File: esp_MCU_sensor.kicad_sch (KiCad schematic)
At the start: 38 parts, among them J4 Conn_01x04_Pin, SW1 SW_Push, U1 ESP32-S3, U2 MX25L6433FM2I-08G, U3 ESP-PSRAM32, U4 BMI323, Y1 Crystal_GND24

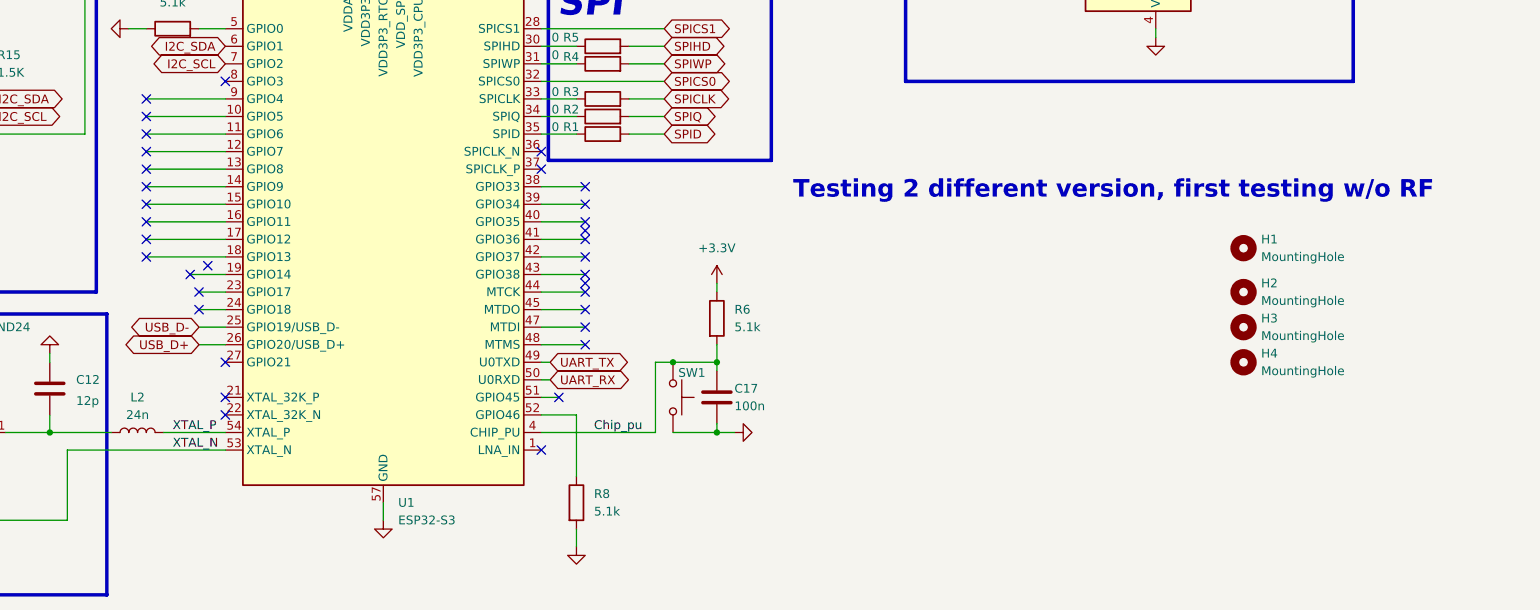
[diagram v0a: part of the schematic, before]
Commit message: Add RF schematics for GPS + designed Pi filter for imp matching
added impedance matching on LNA 1 pin, added GPS/GNSS IC
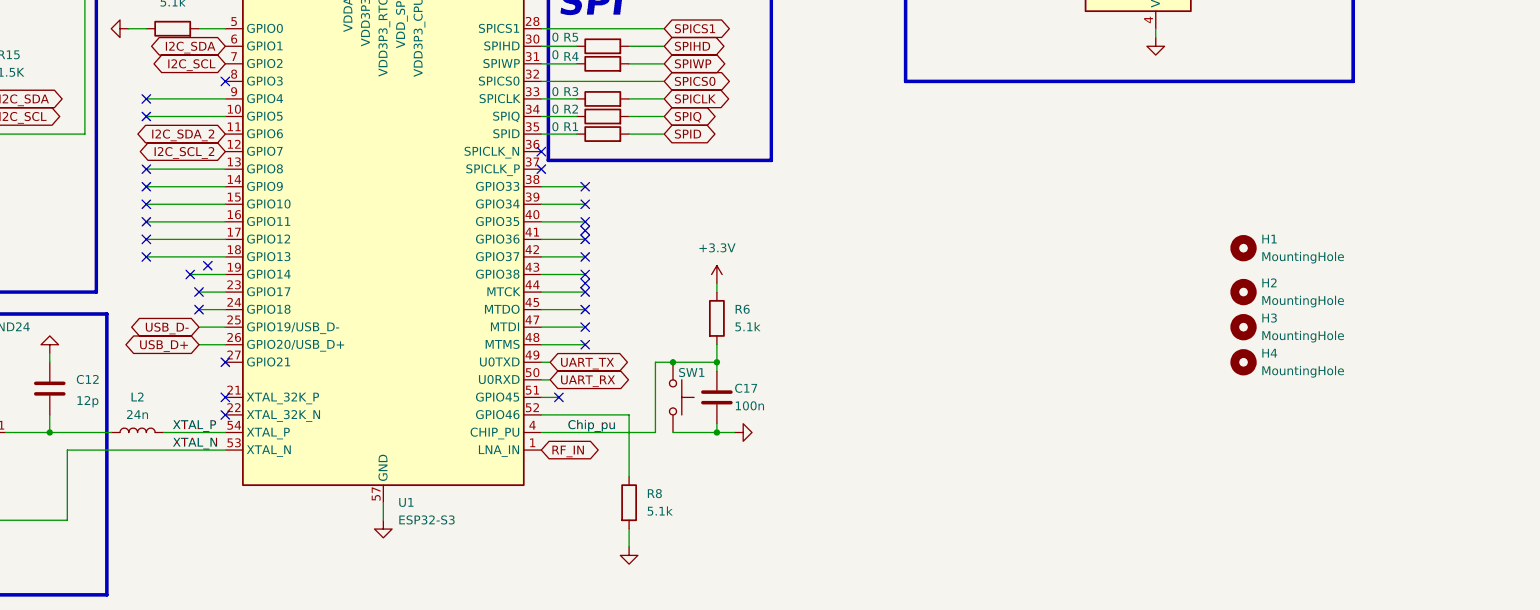
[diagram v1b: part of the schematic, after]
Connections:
- net RF_IN: now reaches U1.1 (LNA_IN)
- net I2C_SDA_2: now reaches U1.11 (GPIO6)
- net I2C_SCL_2: now reaches U1.12 (GPIO7)
- no-connect marks 36 -> 33
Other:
- note removed: "Testing 2 different version, first testing w/o RF"
- moved on the sheet: R8
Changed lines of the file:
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@@
 		)
 	)
-	(text "Testing 2 different version, first testing w/o RF\n"
-		(exclude_from_sim no)
-		(at 232.664 110.998 0)
-		(effects
-			(font
-				(size 2.54 2.54)
-				(thickness 0.508)
-				(bold yes)
-			)
-		)
-	)
 	(text "500mA\n"
 		(exclude_from_sim no)
@@
 	)
 	(no_connect
-		(at 92.71 105.41)
-	)
-	(no_connect
 		(at 64.77 110.49)
 	)
@@
 	)
 	(no_connect
-		(at 149.86 148.59)
-	)
-	(no_connect
 		(at 100.33 128.27)
 	)
 	(no_connect
-		(at 92.71 102.87)
-	)
-	(no_connect
 		(at 104.14 135.89)
 	)
@@
 	(wire
 		(pts
-			(xy 154.94 143.51) (xy 154.94 152.4)
+			(xy 162.56 143.51) (xy 162.56 152.4)
 		)
 		(stroke
@@
 	(wire
 		(pts
-			(xy 149.86 143.51) (xy 154.94 143.51)
+			(xy 149.86 143.51) (xy 162.56 143.51)
 		)
 		(stroke
@@
 	(wire
 		(pts
-			(xy 154.94 160.02) (xy 154.94 162.56)
+			(xy 162.56 160.02) (xy 162.56 162.56)
 		)
 		(stroke
@@
 	(wire
 		(pts
-			(xy 92.71 105.41) (xy 104.14 105.41)
-		)
-		(stroke
-			(width 0)
-			(type default)
-		)
-	)
-	(wire
-		(pts
 			(xy 78.74 143.51) (xy 78.74 146.05)
 		)
@@
 	(wire
 		(pts
-			(xy 92.71 102.87) (xy 104.14 102.87)
-		)
-		(stroke
-			(width 0)
-			(type default)
-		)
-	)
-	(wire
-		(pts
 			(xy 104.14 148.59) (xy 81.28 148.59)
 		)
@@
 	)
 	(label "Chip_pu"
-		(at 157.48 146.05 0)
+		(at 153.67 146.05 0)
 		(effects
 			(font
@@
 		)
 	)
+	(global_label "RF_IN"
+		(shape bidirectional)
+		(at 149.86 148.59 0)
+		(fields_autoplaced yes)
+		(effects
+			(font
+				(size 1.27 1.27)
+			)
+			(justify left)
+		)
+		(property "Intersheetrefs" "${INTERSHEET_REFS}"
+			(at 159.218 148.59 0)
+			(effects
+				(font
+					(size 1.27 1.27)
+				)
+				(justify left)
+				(hide yes)
+			)
+		)
+	)
 	(global_label "SPICLK"
 		(shape bidirectional)
@@
 		)
 	)
+	(global_label "I2C_SDA_2"
+		(shape bidirectional)
+		(at 104.14 102.87 180)
+		(fields_autoplaced yes)
+		(effects
+			(font
+				(size 1.27 1.27)
+			)
+			(justify right)
+		)
+		(property "Intersheetrefs" "${INTERSHEET_REFS}"
+			(at 90.2464 102.87 0)
+			(effects
+				(font
+					(size 1.27 1.27)
+				)
+				(justify right)
+				(hide yes)
+			)
+		)
+	)
+	(global_label "I2C_SCL_2"
+		(shape bidirectional)
+		(at 104.14 105.41 180)
+		(fields_autoplaced yes)
+		(effects
+			(font
+				(size 1.27 1.27)
+			)
+			(justify right)
+		)
+		(property "Intersheetrefs" "${INTERSHEET_REFS}"
+			(at 90.3069 105.41 0)
+			(effects
+				(font
+					(size 1.27 1.27)
+				)
+				(justify right)
+				(hide yes)
+			)
+		)
+	)
 	(global_label "I2C_SCL"
 		(shape bidirectional)
@@
 	(symbol
 		(lib_id "power:GND")
-		(at 154.94 162.56 0)
+		(at 162.56 162.56 0)
 		(unit 1)
 		(exclude_from_sim no)
@@
 		(fields_autoplaced yes)
 		(property "Reference" "#PWR032"
-			(at 154.94 168.91 0)
+			(at 162.56 168.91 0)
 			(effects
 				(font
@@
 		)
 		(property "Value" "GND"
-			(at 154.94 167.64 0)
+			(at 162.56 167.64 0)
 			(effects
 				(font
@@
 		)
 		(property "Footprint" ""
-			(at 154.94 162.56 0)
+			(at 162.56 162.56 0)
 			(effects
 				(font
@@
 		)
 		(property "Datasheet" ""
-			(at 154.94 162.56 0)
+			(at 162.56 162.56 0)
 			(effects
 				(font
@@
 		)
 		(property "Description" "Power symbol creates a global label with name \"GND\" , ground"
-			(at 154.94 162.56 0)
+			(at 162.56 162.56 0)
 			(effects
 				(font
@@
 	(symbol
 		(lib_id "Device:R")
-		(at 154.94 156.21 0)
+		(at 162.56 156.21 0)
 		(unit 1)
 		(exclude_from_sim no)
@@
 		(fields_autoplaced yes)
 		(property "Reference" "R8"
-			(at 157.48 154.9399 0)
+			(at 165.1 154.9399 0)
 			(effects
 				(font
@@
 		)
 		(property "Value" "5.1k"
-			(at 157.48 157.4799 0)
+			(at 165.1 157.4799 0)
 			(effects
 				(font
@@
 		)
 		(property "Footprint" "Resistor_SMD:R_0402_1005Metric_Pad0.72x0.64mm_HandSolder"
-			(at 153.162 156.21 90)
+			(at 160.782 156.21 90)
 			(effects
 				(font
@@
 		)
 		(property "Datasheet" "~"
-			(at 154.94 156.21 0)
+			(at 162.56 156.21 0)
 			(effects
 				(font
@@
 		)
 		(property "Description" "Resistor"
-			(at 154.94 156.21 0)
+			(at 162.56 156.21 0)
 			(effects
 				(font

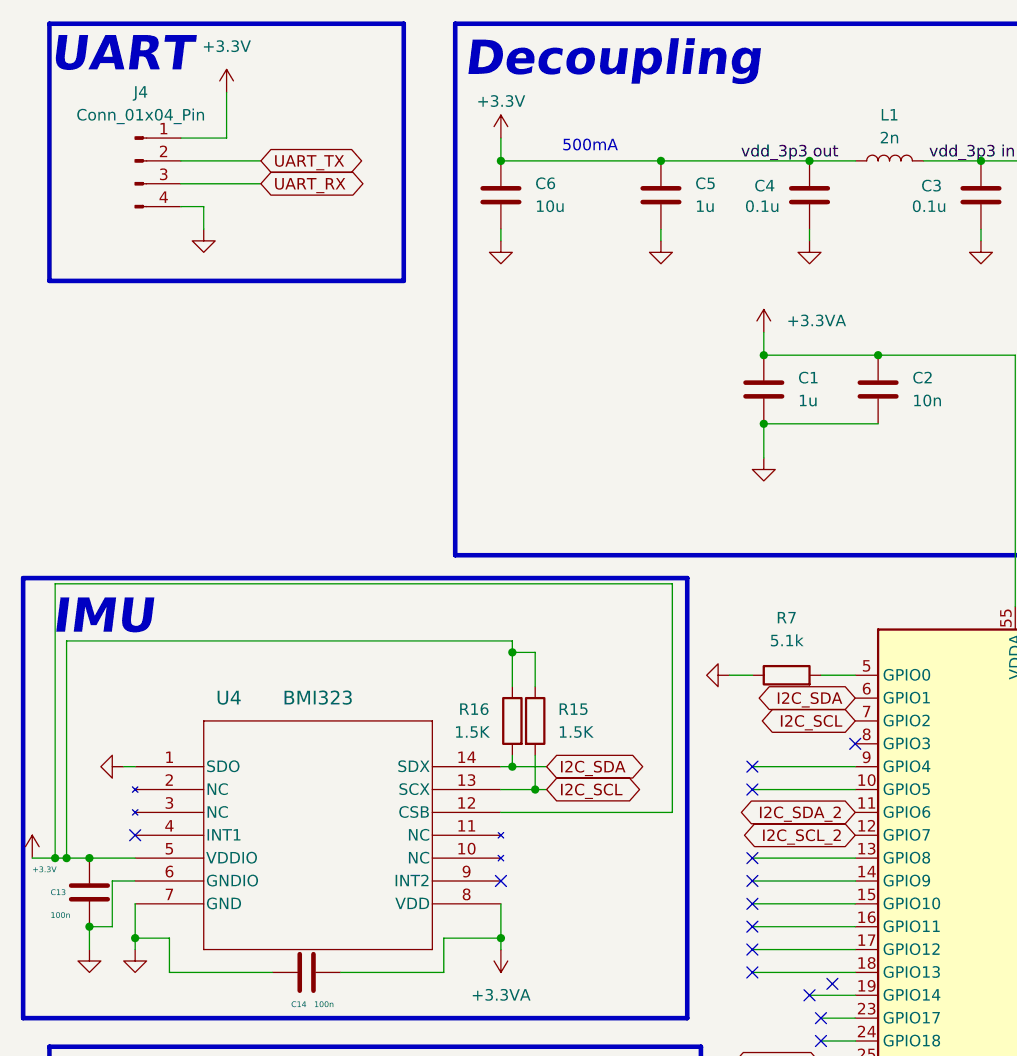
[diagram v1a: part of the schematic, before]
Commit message: Added antenna design
added pcb antenna design
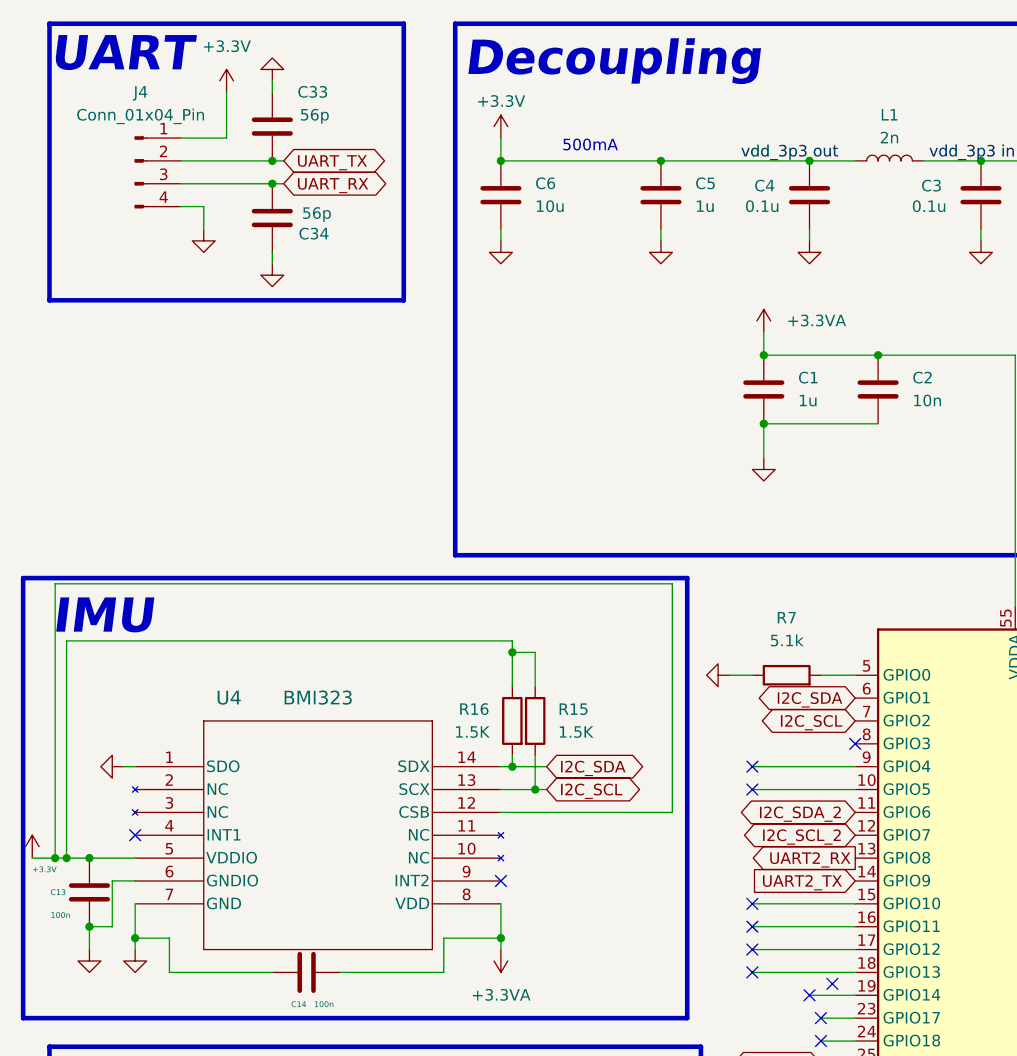
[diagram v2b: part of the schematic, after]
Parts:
- added C33, C34: 56p, Capacitor_SMD:C_0402_1005Metric_Pad0.74x0.62mm_HandSolder, symbol Device:C
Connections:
- net GND: now also C33.1, C34.1
- net UART_RX: now also C34.2
- net UART_TX: now also C33.2
- net UART2_RX: now reaches U1.13 (GPIO8)
- net UART2_TX: now reaches U1.14 (GPIO9)
- no-connect marks 33 -> 31

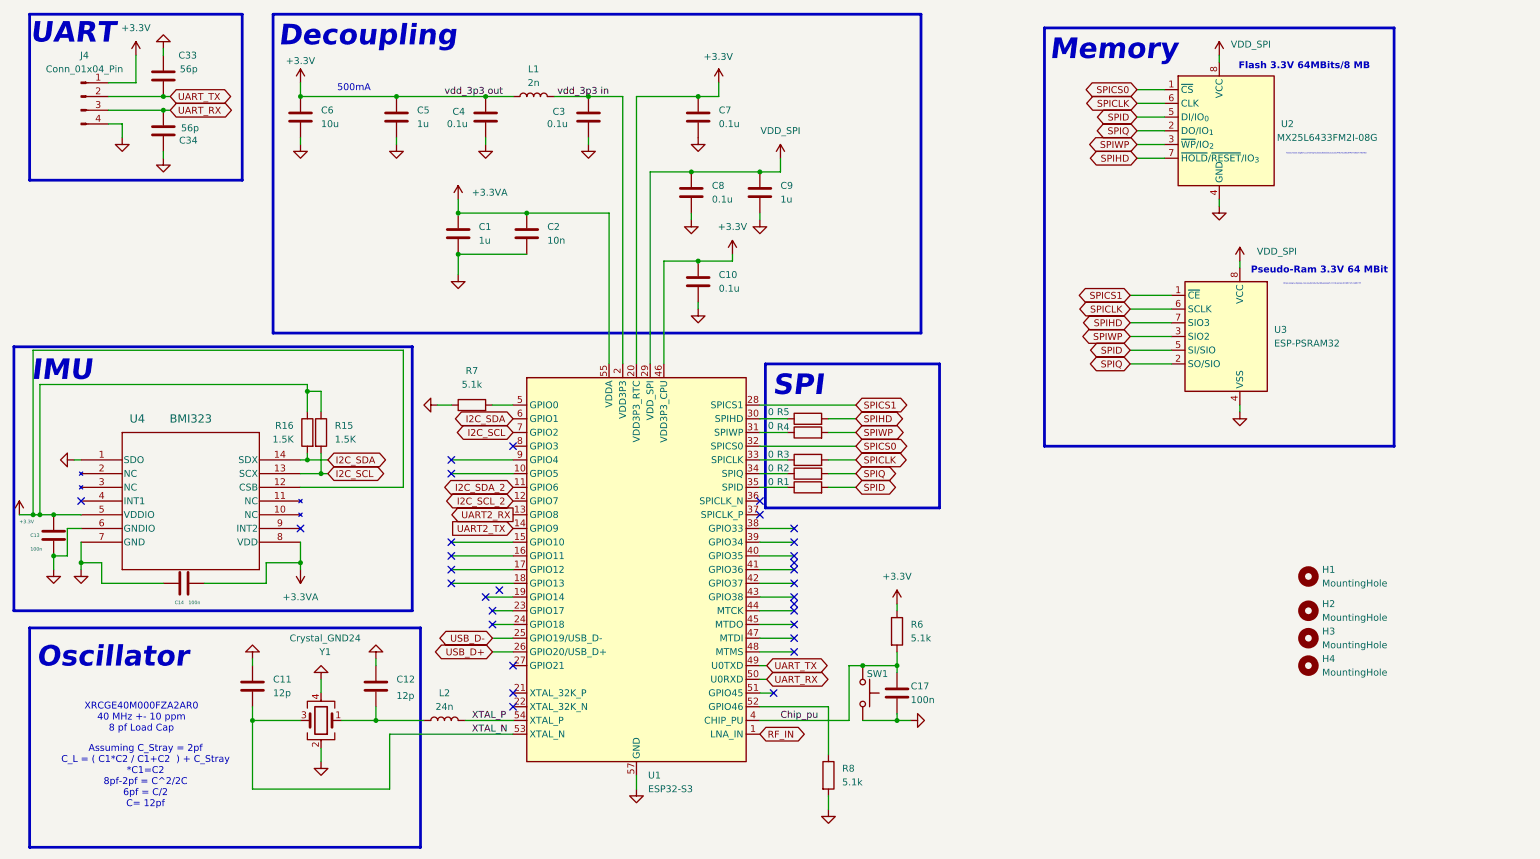
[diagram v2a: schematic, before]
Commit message: placement done
placement done, routing left
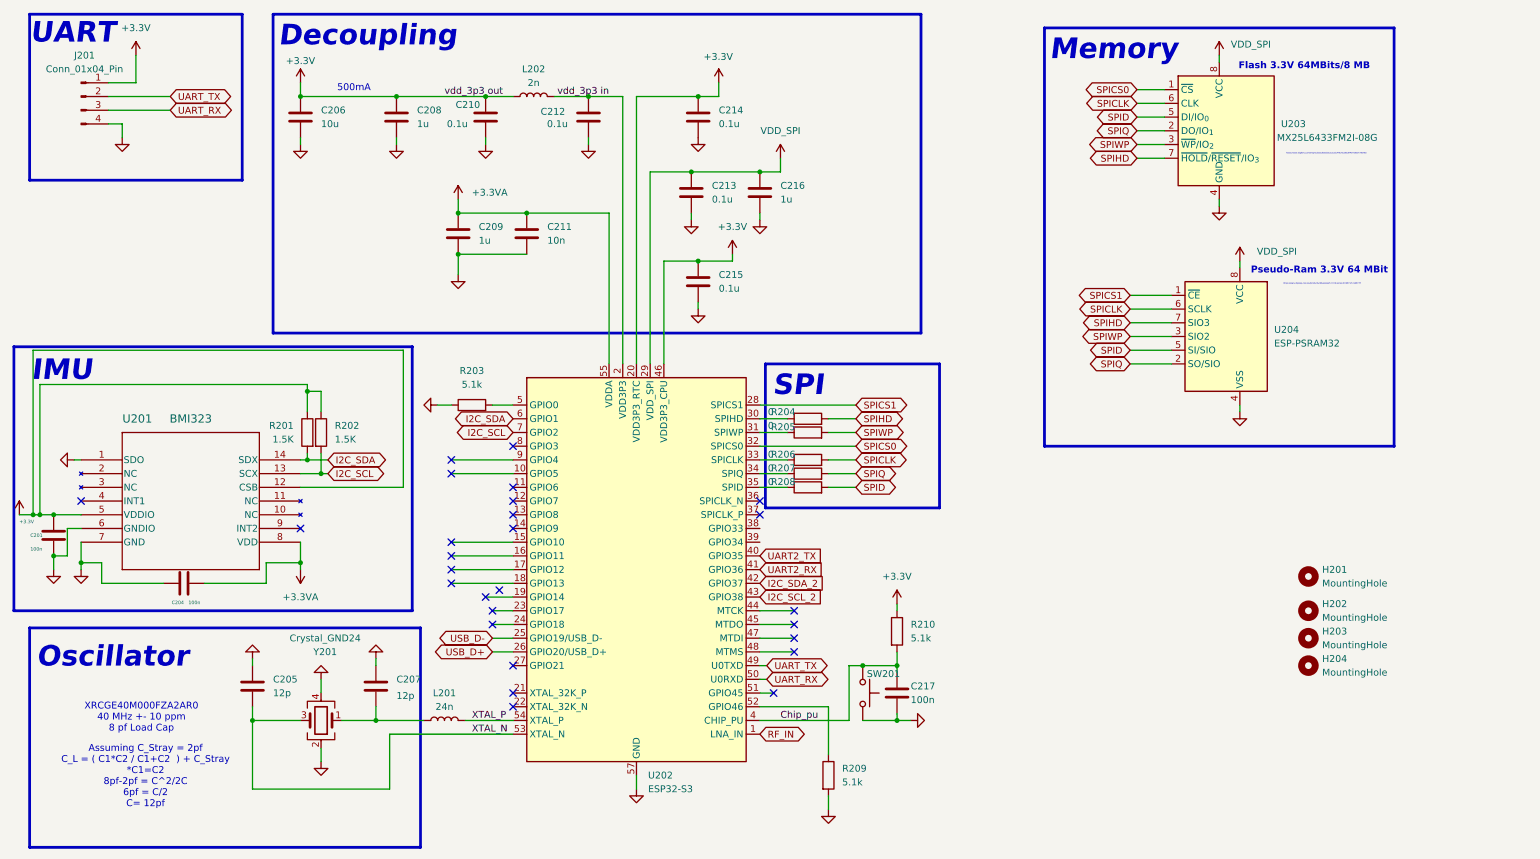
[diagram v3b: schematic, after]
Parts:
- removed C33, C34: 56p, Capacitor_SMD:C_0402_1005Metric_Pad0.74x0.62mm_HandSolder, symbol Device:C
- renumbered C13 to C201, C14 to C204, C11 to C205, C6 to C206, C12 to C207, C5 to C208, C1 to C209, C4 to C210, C2 to C211, C3 to C212, C8 to C213, C7 to C214, C10 to C215, C9 to C216, C17 to C217, H1 to H201, H2 to H202, H3 to H203, H4 to H204, J4 to J201, L2 to L201, L1 to L202, R16 to R201, R15 to R202, R7 to R203, R5 to R204, R4 to R205, R3 to R206, R2 to R207, R1 to R208, R8 to R209, R6 to R210, SW1 to SW201, U4 to U201, U1 to U202, U2 to U203, U3 to U204, Y1 to Y201
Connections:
- net I2C_SCL_2: now also U202.43 (GPIO38); no longer U202.12 (GPIO7)
- net I2C_SDA_2: now also U202.42 (GPIO37); no longer U202.11 (GPIO6)
- net UART2_RX: now also U202.41 (GPIO36); no longer U202.13 (GPIO8)
- net UART2_TX: now also U202.40 (GPIO35); no longer U202.14 (GPIO9)
- no-connect marks 31 -> 27

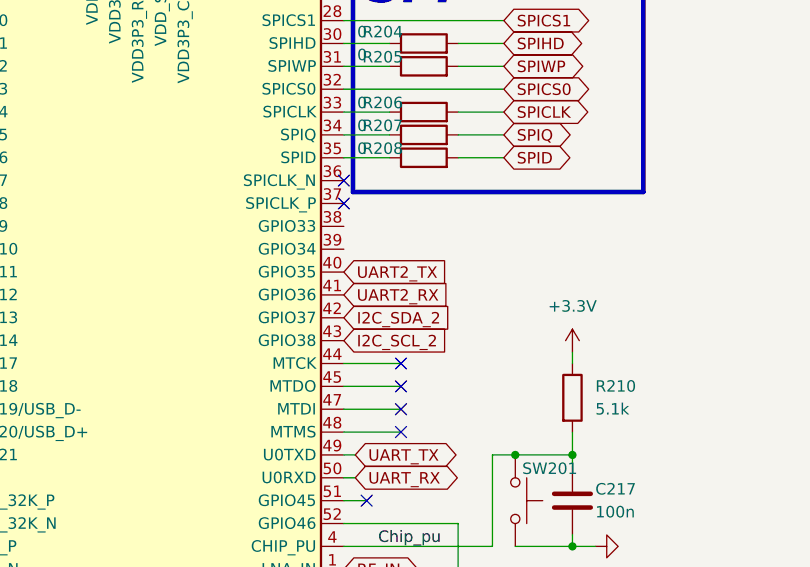
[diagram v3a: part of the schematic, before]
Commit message: finished power routing
finished power routing, gps antenna left
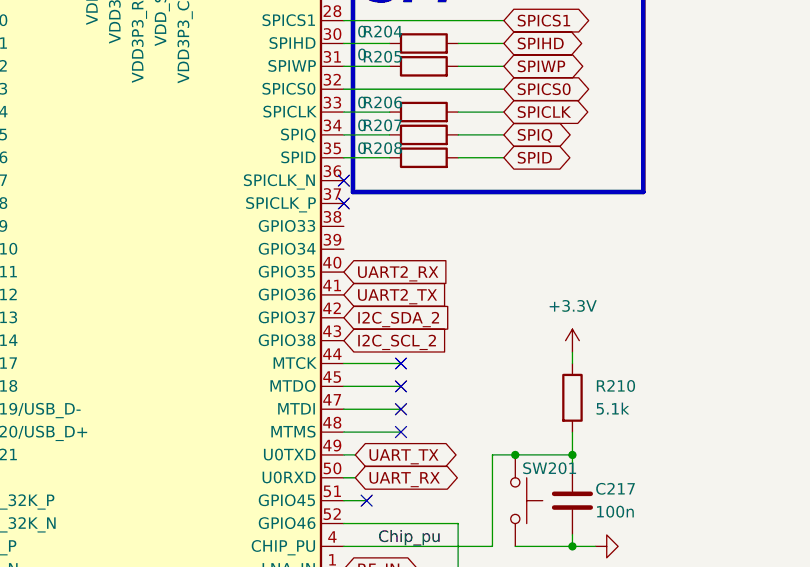
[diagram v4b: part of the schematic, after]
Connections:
- net UART2_RX: now also U202.40 (GPIO35); no longer U202.41 (GPIO36)
- net UART2_TX: now also U202.41 (GPIO36); no longer U202.40 (GPIO35)
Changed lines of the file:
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@@
 	(global_label "UART2_RX"
 		(shape input)
-		(at 149.86 118.11 0)
-		(fields_autoplaced yes)
-		(effects
-			(font
-				(size 1.27 1.27)
-			)
-			(justify left)
-		)
-		(property "Intersheetrefs" "${INTERSHEET_REFS}"
-			(at 162.1585 118.11 0)
+		(at 149.86 115.57 0)
+		(fields_autoplaced yes)
+		(effects
+			(font
+				(size 1.27 1.27)
+			)
+			(justify left)
+		)
+		(property "Intersheetrefs" "${INTERSHEET_REFS}"
+			(at 162.1585 115.57 0)
 			(effects
 				(font
@@
 	(global_label "UART2_TX"
 		(shape input)
-		(at 149.86 115.57 0)
-		(fields_autoplaced yes)
-		(effects
-			(font
-				(size 1.27 1.27)
-			)
-			(justify left)
-		)
-		(property "Intersheetrefs" "${INTERSHEET_REFS}"
-			(at 161.8561 115.57 0)
-			(effects
-				(font
+		(at 149.86 118.11 0)
+		(fields_autoplaced yes)
+		(effects
+			(font
+				(size 1.27 1.27)
+			)
+			(justify left)
+		)
+		(property "Intersheetrefs" "${INTERSHEET_REFS}"
+			(at 161.8561 118.11 0)
+			(effects
+				(font

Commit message: minor changes
minor changes
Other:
- title: Motion_Tracker_V0 -> Motion_Tracker_V1
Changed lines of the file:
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@@
 	(paper "A4")
 	(title_block
-		(title "Motion_Tracker_V0")
+		(title "Motion_Tracker_V1")
 		(company "AMTL-CNDE / Flatrim Dreshaj")
 	)
